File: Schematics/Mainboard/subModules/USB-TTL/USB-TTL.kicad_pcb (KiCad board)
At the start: 2 copper layers, 30 x 30 mm, 7 parts, among them J1 Input, J2 Output, Q1 DTC143T, Q2 DTC143T, U1 CH340B

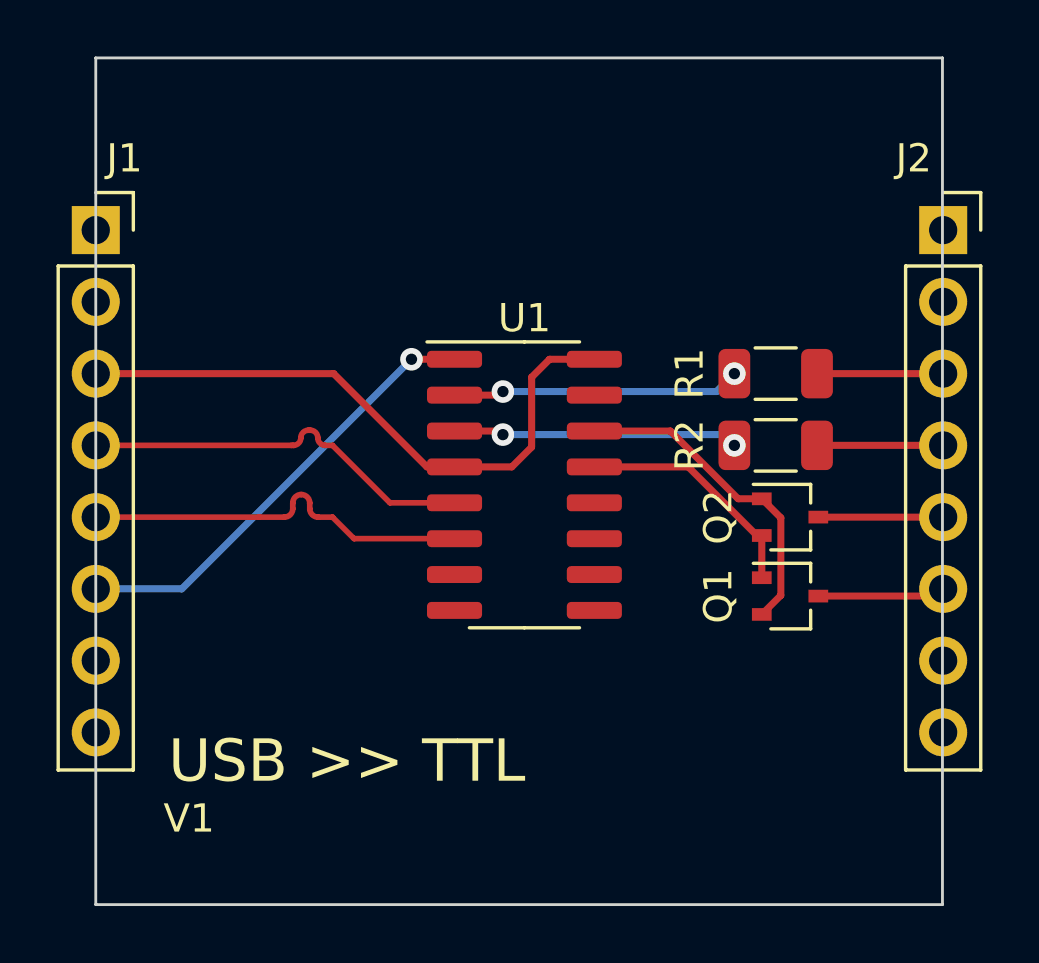
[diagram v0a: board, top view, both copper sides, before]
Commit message: USB-TTL 2cm
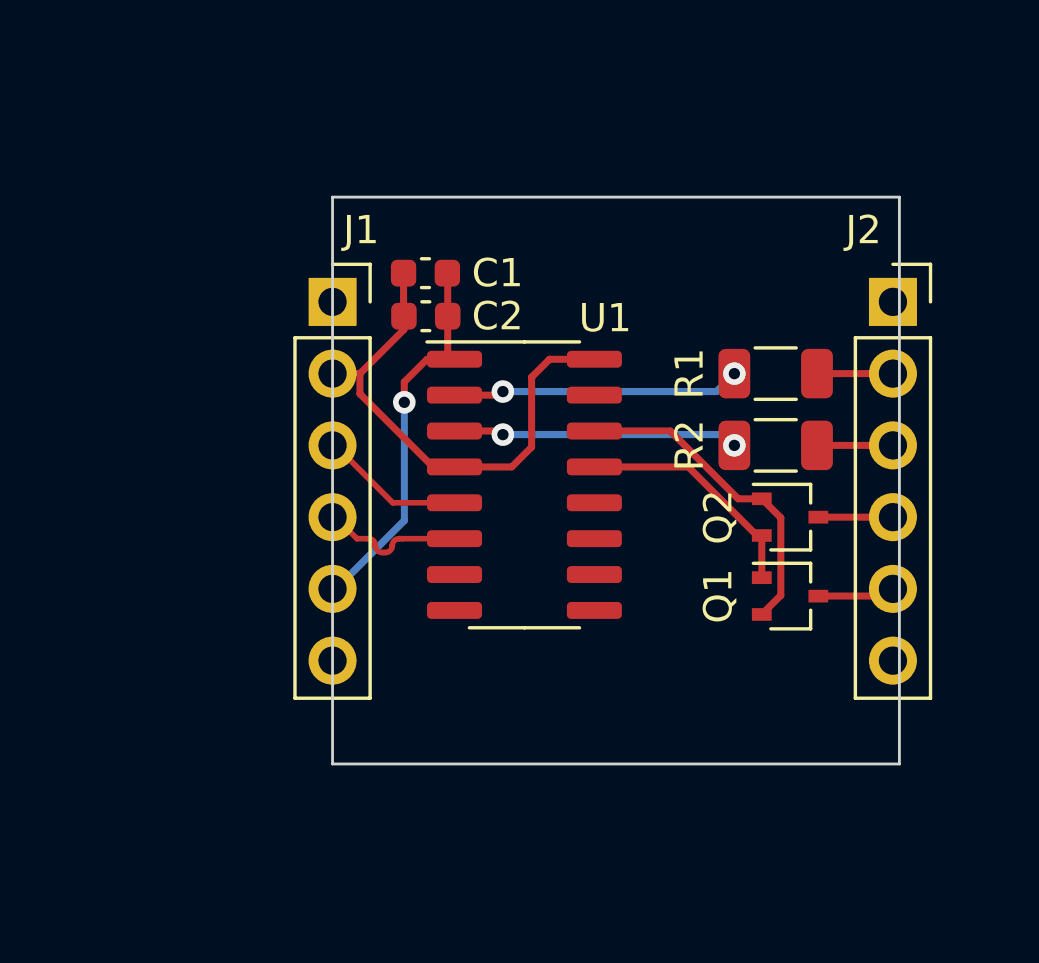
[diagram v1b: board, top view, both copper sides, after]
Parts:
- added C1: 10u, Capacitor_SMD:C_0603_1608Metric, F.Cu at (141.2, 86.4)
- added C2: 0u1, Capacitor_SMD:C_0603_1608Metric, F.Cu at (141.2, 87.9)
- J1, J2: footprint Connector_PinSocket_2.54mm:PinSocket_1x08_P2.54mm_Vertical -> Connector_PinSocket_2.54mm:PinSocket_1x06_P2.54mm_Vertical
- moved J1 8.76 mm to (137.9, 87.4)
- moved J2 3.10 mm to (157.8, 87.4)
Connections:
- J1 pad 2: (no net) -> +3V3
- J1 pad 3: +3V3 -> USB D+
- J1 pad 4: USB D+ -> USB D-
- J1 pad 5: USB D- -> GND
- J1 pad 6: GND -> (no net)
- J2 pad 2: (no net) -> TTL TX
- J2 pad 3: TTL TX -> TTL RX
- J2 pad 4: TTL RX -> IO0
- J2 pad 5: IO0 -> EN
- J2 pad 6: EN -> (no net)
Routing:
- net USB D+: track 14.0 -> 5.06 mm
- net USB D-: track 14.0 -> 5.05 mm
- net +3V3: track 21.9 -> 18.2 mm
- net GND: track 15.9 -> 13.6 mm
- net EN: track 4.82 -> 2.75 mm
- net TTL TX: track 4.32 -> 2.69 mm
- net TTL RX: track 4.32 -> 2.69 mm
- net IO0: track 4.27 -> 2.64 mm
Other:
- board size 30 x 30 mm -> 20.1 x 20.1 mm
- board text removed: "USB >> TTL"
- board text removed: "V1"

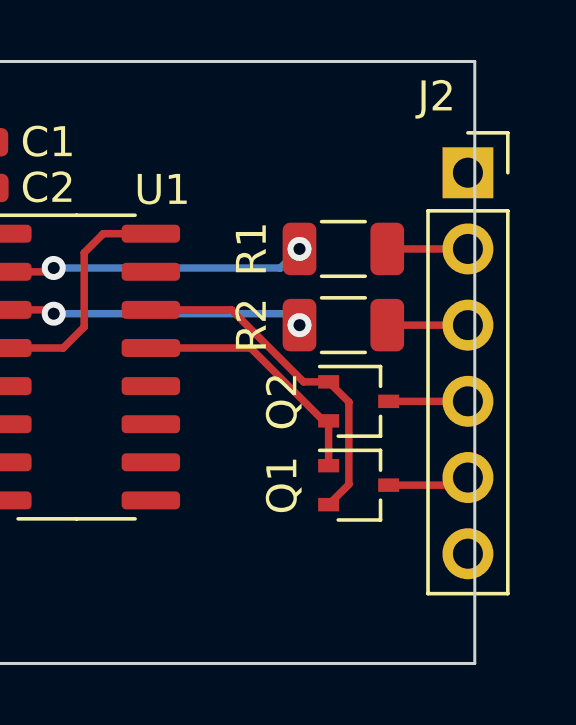
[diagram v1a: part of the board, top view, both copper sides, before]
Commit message: Added USB-TTL gerbers
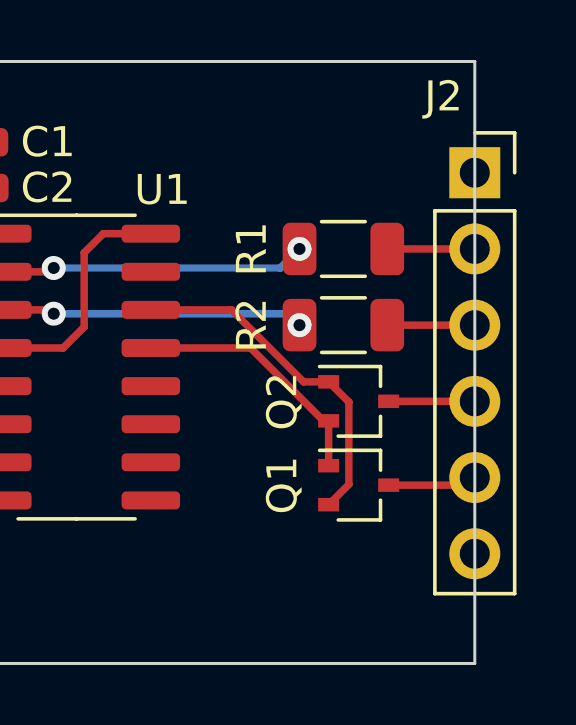
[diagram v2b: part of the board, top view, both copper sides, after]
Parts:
- moved J2 0.23 mm to (158.0, 87.4)
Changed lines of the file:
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@@
   )
   (footprint "Connector_PinSocket_2.54mm:PinSocket_1x06_P2.54mm_Vertical" (layer "F.Cu")
-    (at 157.759 87.376)
+    (at 157.988 87.376)
     (descr "Through hole straight socket strip, 1x06, 2.54mm pitch, single row (from Kicad 4.0.7), script generated")
     (tags "Through hole socket strip THT 1x06 2.54mm single row")
@@
   (arc (start 139.437359 96.00336) (mid 139.509223 96.176855) (end 139.682718 96.248719) (width 0.2) (layer "F.Cu") (net 4))
   (arc (start 140.037359 96.003359) (mid 140.109223 95.829864) (end 140.282718 95.758) (width 0.2) (layer "F.Cu") (net 4))
-  (segment (start 155.071 89.916) (end 157.759 89.916) (width 0.25) (layer "F.Cu") (net 5))
-  (segment (start 155.071 92.456) (end 157.759 92.456) (width 0.25) (layer "F.Cu") (net 6))
-  (segment (start 155.1165 94.996) (end 157.759 94.996) (width 0.25) (layer "F.Cu") (net 7))
-  (segment (start 155.1165 97.79) (end 157.505 97.79) (width 0.25) (layer "F.Cu") (net 8))
+  (segment (start 155.071 89.916) (end 157.86298 89.916) (width 0.25) (layer "F.Cu") (net 5))
+  (segment (start 155.071 92.456) (end 157.86298 92.456) (width 0.25) (layer "F.Cu") (net 6))
+  (segment (start 155.1165 94.996) (end 157.86298 94.996) (width 0.25) (layer "F.Cu") (net 7))
+  (segment (start 155.1165 97.79) (end 157.60898 97.79) (width 0.25) (layer "F.Cu") (net 8))
+  (segment (start 157.60898 97.79) (end 157.86298 97.536) (width 0.25) (layer "F.Cu") (net 8))
   (segment (start 157.505 97.79) (end 157.759 97.536) (width 0.25) (layer "F.Cu") (net 8))
   (segment (start 153.1165 97.14) (end 153.1165 95.646) (width 0.25) (layer "F.Cu") (net 9))
